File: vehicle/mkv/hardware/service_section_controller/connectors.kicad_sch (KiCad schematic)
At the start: 4 parts

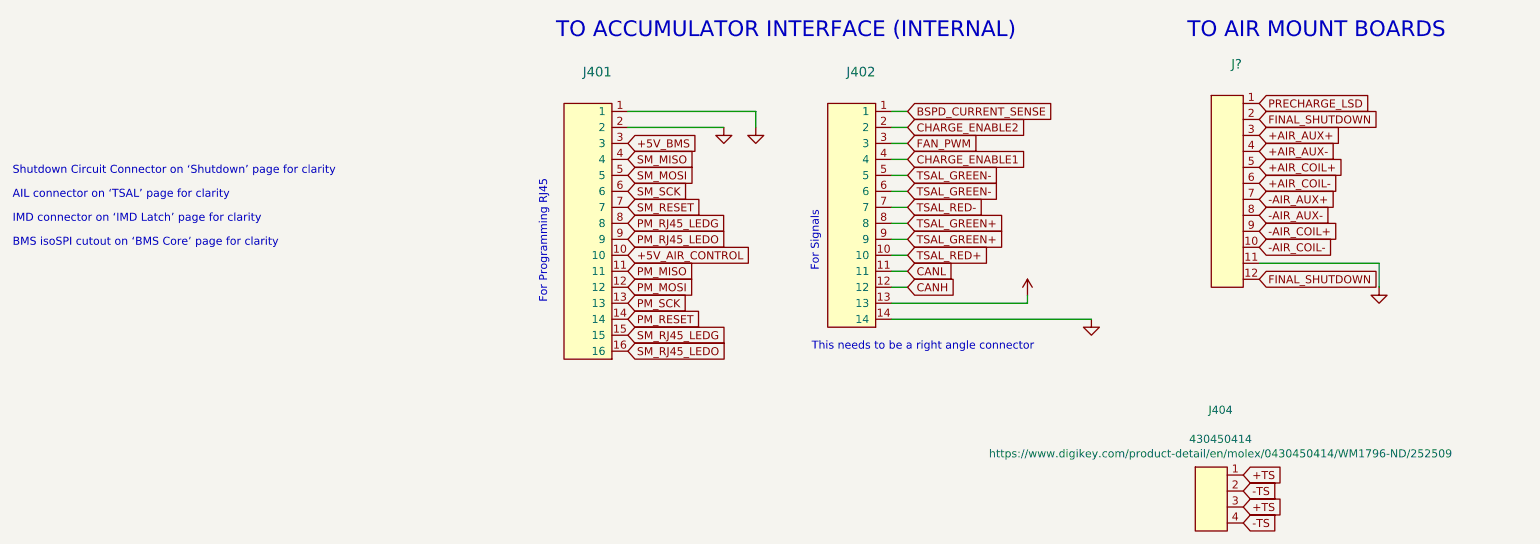
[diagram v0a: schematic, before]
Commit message: chore: annotate migrated schematics
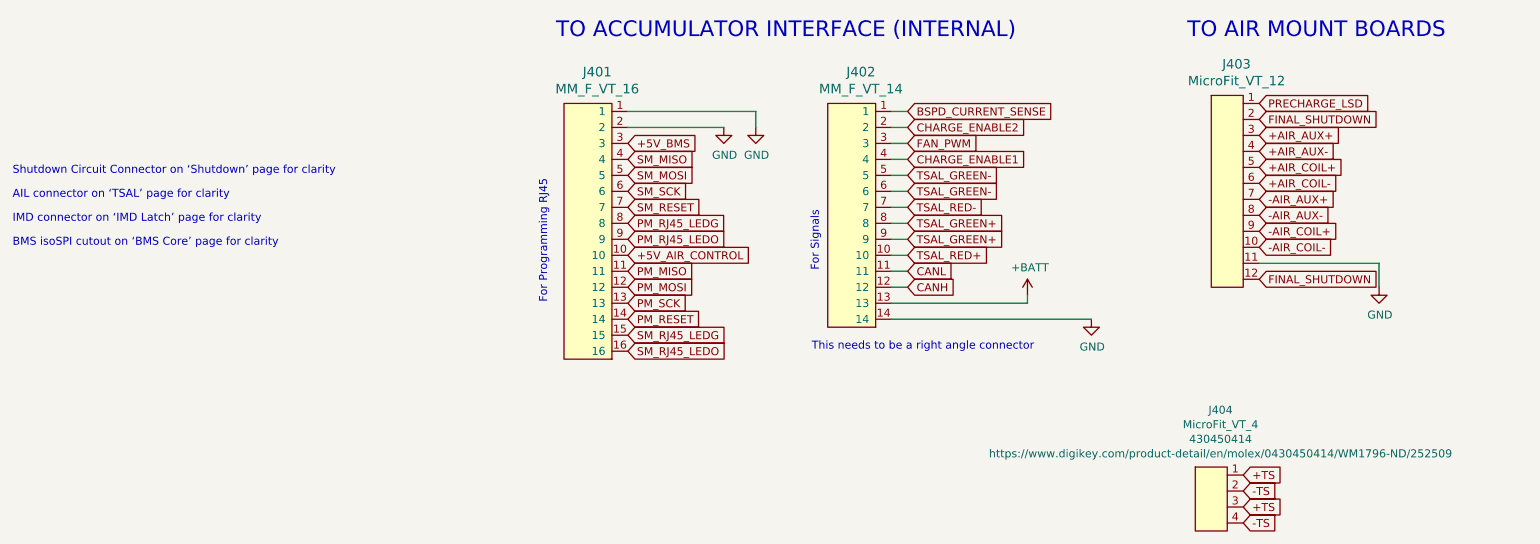
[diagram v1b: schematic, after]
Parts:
- J401: value (none) -> MM_F_VT_16; footprint (none) -> footprints:micromatch_female_vert_16
- J402: value (none) -> MM_F_VT_14; footprint (none) -> footprints:micromatch_female_vert_14
- J403: renamed from J?; value (none) -> MicroFit_VT_12; footprint (none) -> footprints:MicroFit_VT_12
- J404: value (none) -> MicroFit_VT_4; footprint (none) -> footprints:MicroFit_VT_4
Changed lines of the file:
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@@
       (effects (font (size 1.524 1.524)))
     )
-    (property "Value" "" (id 1) (at 124.6632 40.8686 0)
+    (property "Value" "MM_F_VT_16" (id 1) (at 124.6632 40.8686 0)
       (effects (font (size 1.524 1.524)))
     )
-    (property "Footprint" "" (id 2) (at 120.65 44.45 0)
+    (property "Footprint" "footprints:micromatch_female_vert_16" (id 2) (at 120.65 44.45 0)
       (effects (font (size 1.524 1.524)) hide)
     )
@@
       (effects (font (size 1.27 1.27)) hide)
     )
-    (property "Value" "" (id 1) (at 249.047 76.7842 0))
+    (property "Value" "GND" (id 1) (at 249.047 76.7842 0))
     (property "Footprint" "" (id 2) (at 248.92 72.39 0)
       (effects (font (size 1.27 1.27)) hide)
@@
   (symbol (lib_id "formula:MicroFit_VT_12") (at 224.79 57.15 0) (unit 1)
     (in_bom yes) (on_board yes)
-    (property "Reference" "J?" (id 0) (at 226.2632 36.9316 0)
+    (property "Reference" "J403" (id 0) (at 226.2632 36.9316 0)
       (effects (font (size 1.4986 1.4986)))
     )
-    (property "Value" "" (id 1) (at 226.2632 39.5986 0)
+    (property "Value" "MicroFit_VT_12" (id 1) (at 226.2632 39.5986 0)
       (effects (font (size 1.4986 1.4986)))
     )
-    (property "Footprint" "" (id 2) (at 224.79 76.2 0)
+    (property "Footprint" "footprints:MicroFit_VT_12" (id 2) (at 224.79 76.2 0)
       (effects (font (size 2.54 2.54)) hide)
     )
@@
       (effects (font (size 1.27 1.27)) hide)
     )
-    (property "Value" "" (id 1) (at 144.907 51.3842 0))
+    (property "Value" "GND" (id 1) (at 144.907 51.3842 0))
     (property "Footprint" "" (id 2) (at 144.78 46.99 0)
       (effects (font (size 1.27 1.27)) hide)
@@
       (effects (font (size 1.27 1.27)) hide)
     )
-    (property "Value" "" (id 1) (at 149.987 51.3842 0))
+    (property "Value" "GND" (id 1) (at 149.987 51.3842 0))
     (property "Footprint" "" (id 2) (at 149.86 46.99 0)
       (effects (font (size 1.27 1.27)) hide)
@@
       (effects (font (size 1.27 1.27)) hide)
     )
-    (property "Value" "" (id 1) (at 203.327 81.8642 0))
+    (property "Value" "GND" (id 1) (at 203.327 81.8642 0))
     (property "Footprint" "" (id 2) (at 203.2 77.47 0)
       (effects (font (size 1.27 1.27)) hide)
@@
       (effects (font (size 1.524 1.524)))
     )
-    (property "Value" "" (id 1) (at 166.5732 40.8686 0)
+    (property "Value" "MM_F_VT_14" (id 1) (at 166.5732 40.8686 0)
       (effects (font (size 1.524 1.524)))
     )
-    (property "Footprint" "" (id 2) (at 162.56 44.45 0)
+    (property "Footprint" "footprints:micromatch_female_vert_14" (id 2) (at 162.56 44.45 0)
       (effects (font (size 1.524 1.524)) hide)
     )
@@
       (effects (font (size 1.27 1.27)) hide)
     )
-    (property "Value" "" (id 1) (at 193.421 69.2658 0))
+    (property "Value" "+BATT" (id 1) (at 193.421 69.2658 0))
     (property "Footprint" "" (id 2) (at 193.04 73.66 0)
       (effects (font (size 1.27 1.27)) hide)
@@
     (in_bom yes) (on_board yes)
     (property "Reference" "J404" (id 0) (at 223.7232 91.8972 0))
-    (property "Value" "" (id 1) (at 223.7232 94.2086 0))
-    (property "Footprint" "" (id 2) (at 222.25 113.665 0)
+    (property "Value" "MicroFit_VT_4" (id 1) (at 223.7232 94.2086 0))
+    (property "Footprint" "footprints:MicroFit_VT_4" (id 2) (at 222.25 113.665 0)
       (effects (font (size 1.27 1.27)) hide)
     )
